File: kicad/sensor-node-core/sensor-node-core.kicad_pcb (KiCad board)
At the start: 2 copper layers, 29.5 x 48.3 mm, 18 parts, among them SW1 SW_Push

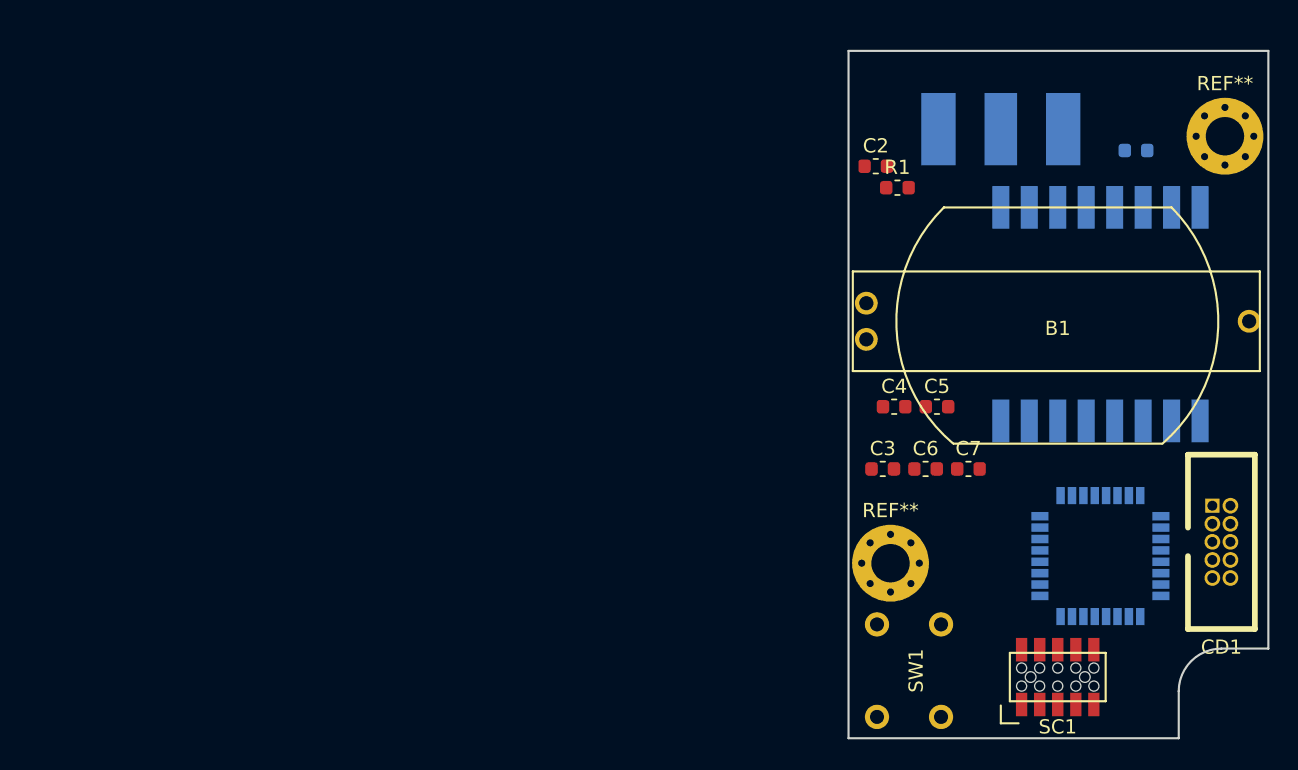
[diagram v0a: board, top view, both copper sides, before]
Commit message: updated switch model and layout
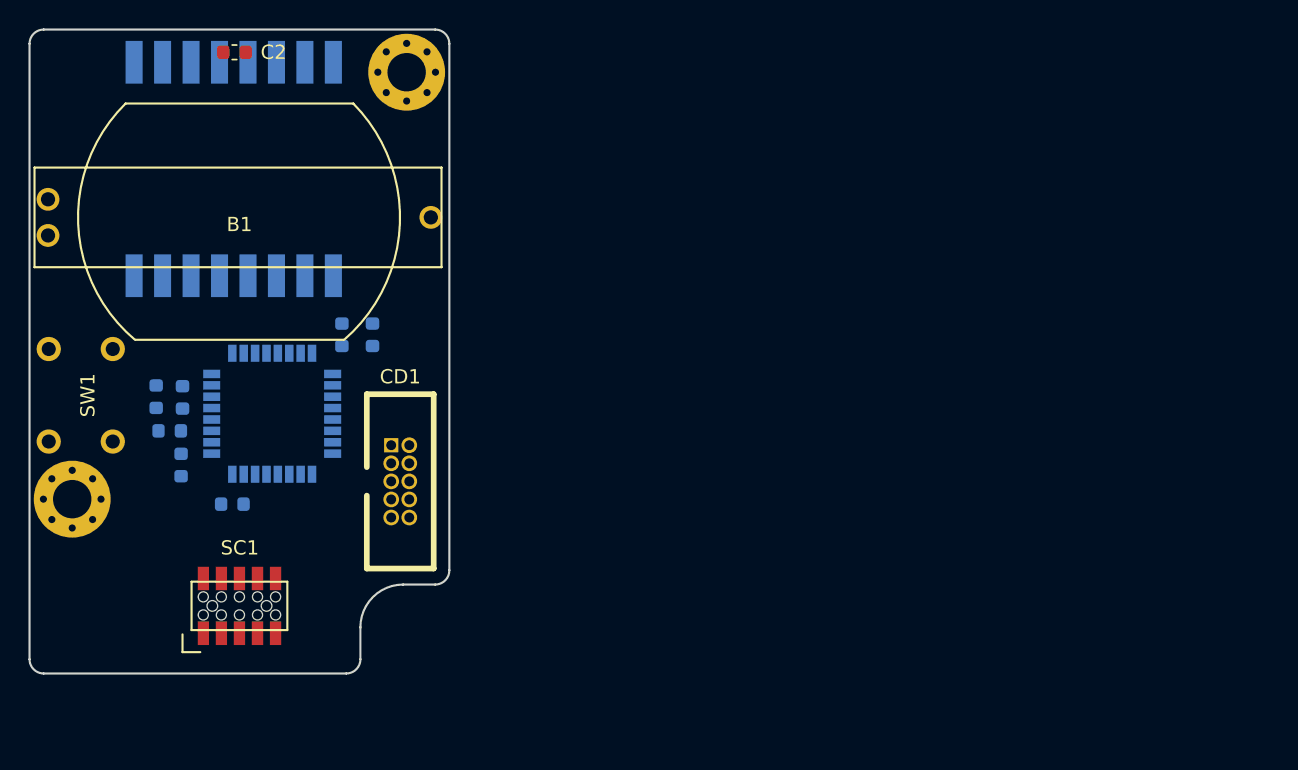
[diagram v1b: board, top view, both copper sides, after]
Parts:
- removed AE1: Antenna_Shield, sensor-node-core:MOLEX-0732511150
- removed the REF** at (195.8, 119.5)
- removed the REF** at (219.2, 89.5)
- added REF**: MountingHole_2.7mm_M2.5_Pad_Via, official stable:MountingHole_2.7mm_M2.5_Pad_Via, F.Cu at (138.2, 115.0)
- added REF**: MountingHole_2.7mm_M2.5_Pad_Via, official stable:MountingHole_2.7mm_M2.5_Pad_Via, F.Cu at (161.8, 85.0)
- C3, C4, C5, C6, C7, R1: moved to B.Cu
- moved C1 70.7 mm to (145.1, 110.2), turned to 180 degrees
- moved RFM1 61.7 mm to (149.6, 91.8)
- moved SW1 61.3 mm to (138.8, 107.7)
- moved STM1 59.1 mm to (152.3, 109.0)
- moved B1 58.0 mm to (150.0, 95.2)
- moved CD1 57.9 mm to (161.3, 113.8)
- moved SC1 57.7 mm to (150.0, 122.5)
- moved REF** 57.7 mm to (150.0, 100.0)
- moved C5 53.3 mm to (145.9, 112.6), turned to 90 degrees
- moved R1 51.8 mm to (149.5, 115.3), turned to 180 degrees
- moved C3 51.3 mm to (144.2, 107.8), turned to 90 degrees
- moved C4 50.0 mm to (146.0, 107.8), turned to 90 degrees
- moved C2 45.8 mm to (149.7, 83.6), turned to 180 degrees
- moved C7 42.9 mm to (159.3, 103.5), turned to 90 degrees
- moved C6 42.1 mm to (157.2, 103.5), turned to 90 degrees
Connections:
- RFM1 pad 9: Net-(AE1-Pad1) -> (no net)
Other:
- board size 29.5 x 48.3 mm -> 29.5 x 45.2 mm

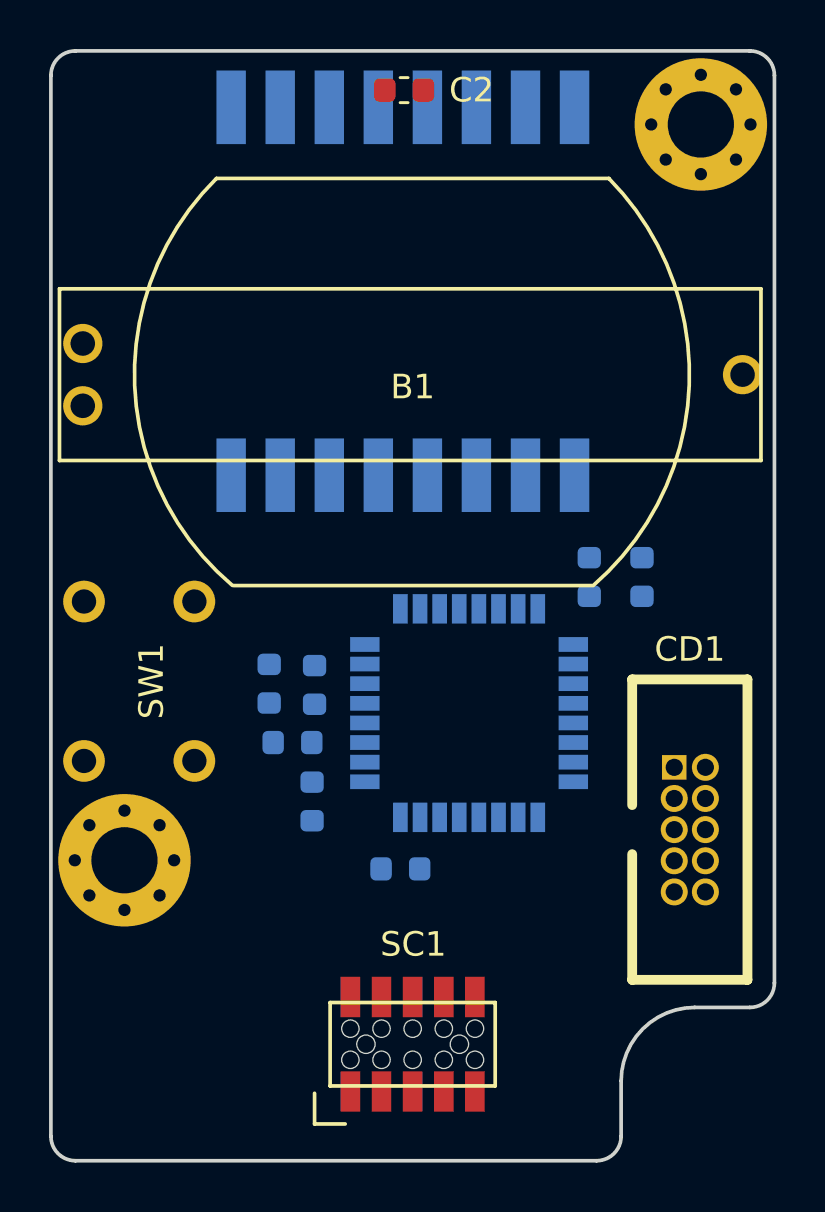
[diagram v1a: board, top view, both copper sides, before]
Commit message: added firmware folder and routing
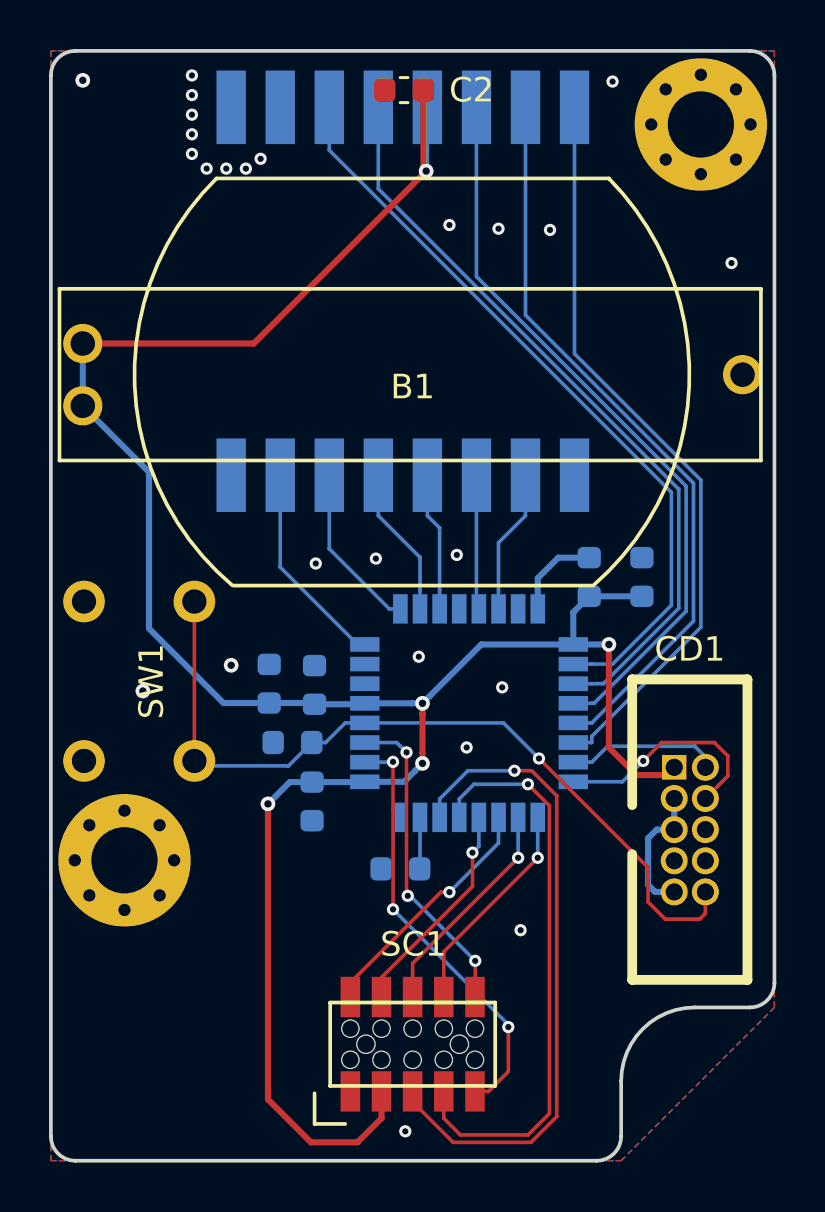
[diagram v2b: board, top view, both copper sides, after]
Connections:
- C1 pad 1: /~SWD_RESET -> /~SWD_RST
- C5 pad 2: Net-(C5-Pad2) -> /3V3
- CD1 pad 10: (no net) -> /~SWD_RST
- SC1 pad 10: (no net) -> /SEN_GPIO_2
- SC1 pad 2: (no net) -> /SEN_SPI_MISO
- SC1 pad 4: (no net) -> /SEN_SPI_MOSI
- SC1 pad 6: (no net) -> /SEN_SPI_CLK
- SC1 pad 8: (no net) -> /~SEN_SPI_CS
- SC1 pad 9: (no net) -> /SEN_GPIO_1
- STM1 pad 1: Net-(C5-Pad2) -> /3V3
- STM1 pad 2: (no net) -> /SEN_GPIO_1
- STM1 pad 25: (no net) -> /~SEN_SPI_CS
- STM1 pad 26: (no net) -> /SEN_SPI_CLK
- STM1 pad 27: (no net) -> /SEN_SPI_MISO
- STM1 pad 28: (no net) -> /SEN_SPI_MOSI
- STM1 pad 3: (no net) -> /SEN_GPIO_2
- STM1 pad 4: /~SWD_RESET -> /~SWD_RST
- SW1 pad 2: /~SWD_RESET -> /~SWD_RST
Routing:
- net /3V3: track 0.00 -> 96.8 mm, vias 0 -> 5
- net /~SWD_RST: track 0.00 -> 33.2 mm, vias 0 -> 1
- net /RFM_DIO4: track 0.00 -> 31.1 mm
- net /RFM_DIO3: track 0.00 -> 31.1 mm
- net /RFM_DIO2: track 0.00 -> 30.6 mm
- net /RFM_DIO1: track 0.00 -> 30.4 mm
- net /RFM_DIO0: track 0.00 -> 30.2 mm
- net /SEN_I2C_SDA: track 0.00 -> 26.9 mm, vias 0 -> 1
- net /SEN_I2C_SCL: track 0.00 -> 23.6 mm, vias 0 -> 1
- net /SEN_GPIO_1: track 0.00 -> 17.4 mm, vias 0 -> 3
- net /SEN_GPIO_2: track 0.00 -> 13.1 mm, vias 0 -> 3
- net /SEN_SPI_MISO: track 0.00 -> 10.0 mm, vias 0 -> 1
- net /SWD_CLK: track 0.00 -> 9.30 mm, vias 0 -> 1
- net GND: track 0.00 -> 9.26 mm, vias 0 -> 25
- net /SEN_SPI_CLK: track 0.00 -> 9.11 mm, vias 0 -> 1
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- added copper zone on B.Cu, net GND
- added copper zone on F.Cu, net GND
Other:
- net class Default: clearance 0.2 -> 0.1; trace_width 0.25 -> 0.15; via_dia 0.8 -> 0.5; via_drill 0.4 -> 0.25
- net class Power added: clearance 0.2, trace_width 0.25, via_dia 0.6, via_drill 0.3
- rule trace_clearance: 0.2 -> 0.1
- rule trace_min: 0.2 -> 0.1
- rule via_min_drill: 0.3 -> 0.2
- rule via_min_size: 0.4 -> 0.45

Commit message: added label and logo
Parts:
- added G***: LOGO, sensor-node-core:logo, F.Cu at (150.0, 112.0)
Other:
- board text added: "hochreiner.net sensor-node-core"
